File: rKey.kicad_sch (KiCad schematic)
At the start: 39 parts, among them IC1 BDX34C, J1 Conn_01x06, Q1 BC337, Q2 BC337, Q3 BC337, Q4 BC337, Q5 BC327, Q8 BC337, U1 TL084BCN, U2 LM7810_TO220

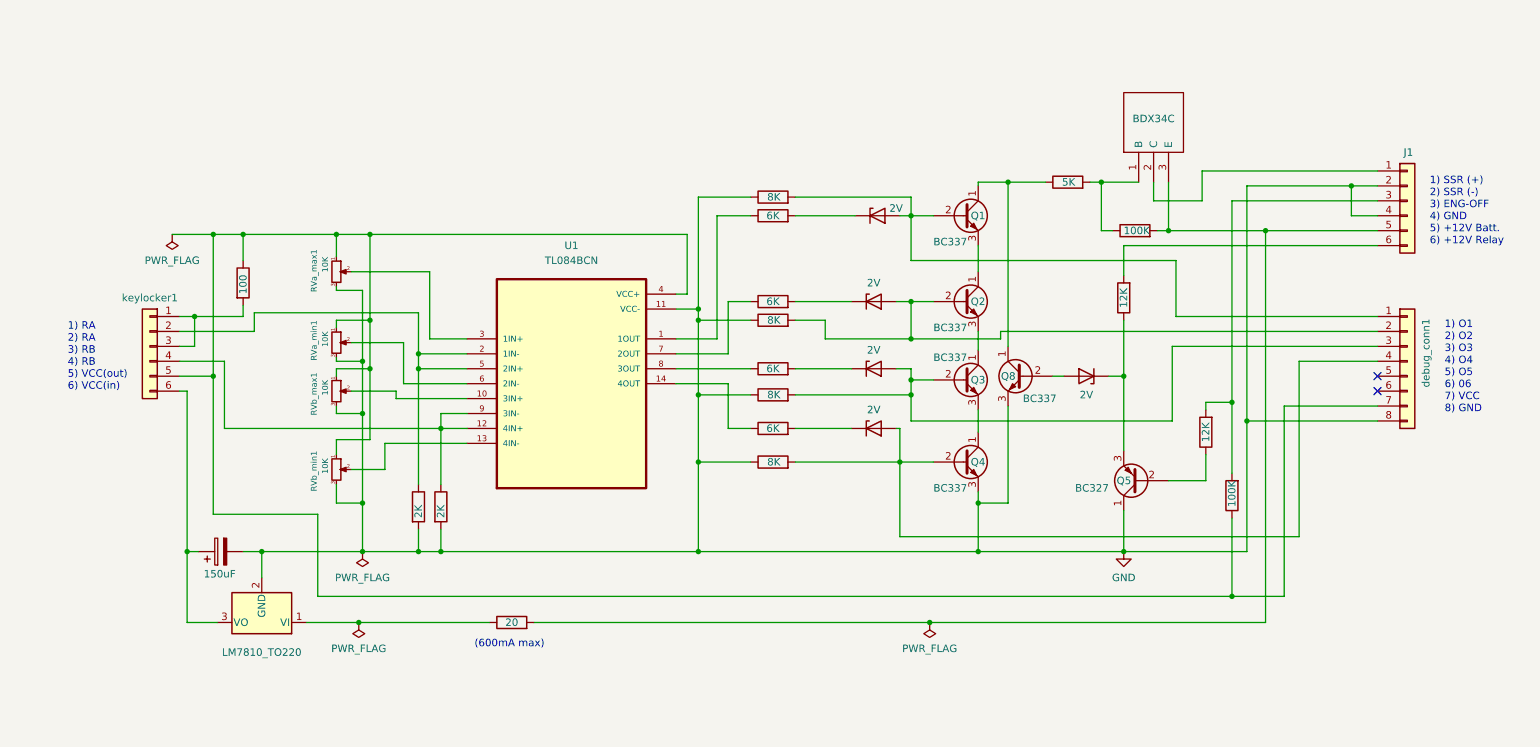
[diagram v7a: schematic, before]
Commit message: feat: Locking the engine when the vehicle is off
In order to forbid to manually run the engine when the vehicle is off, I added a NC micro relay.
PCB size has been reduced
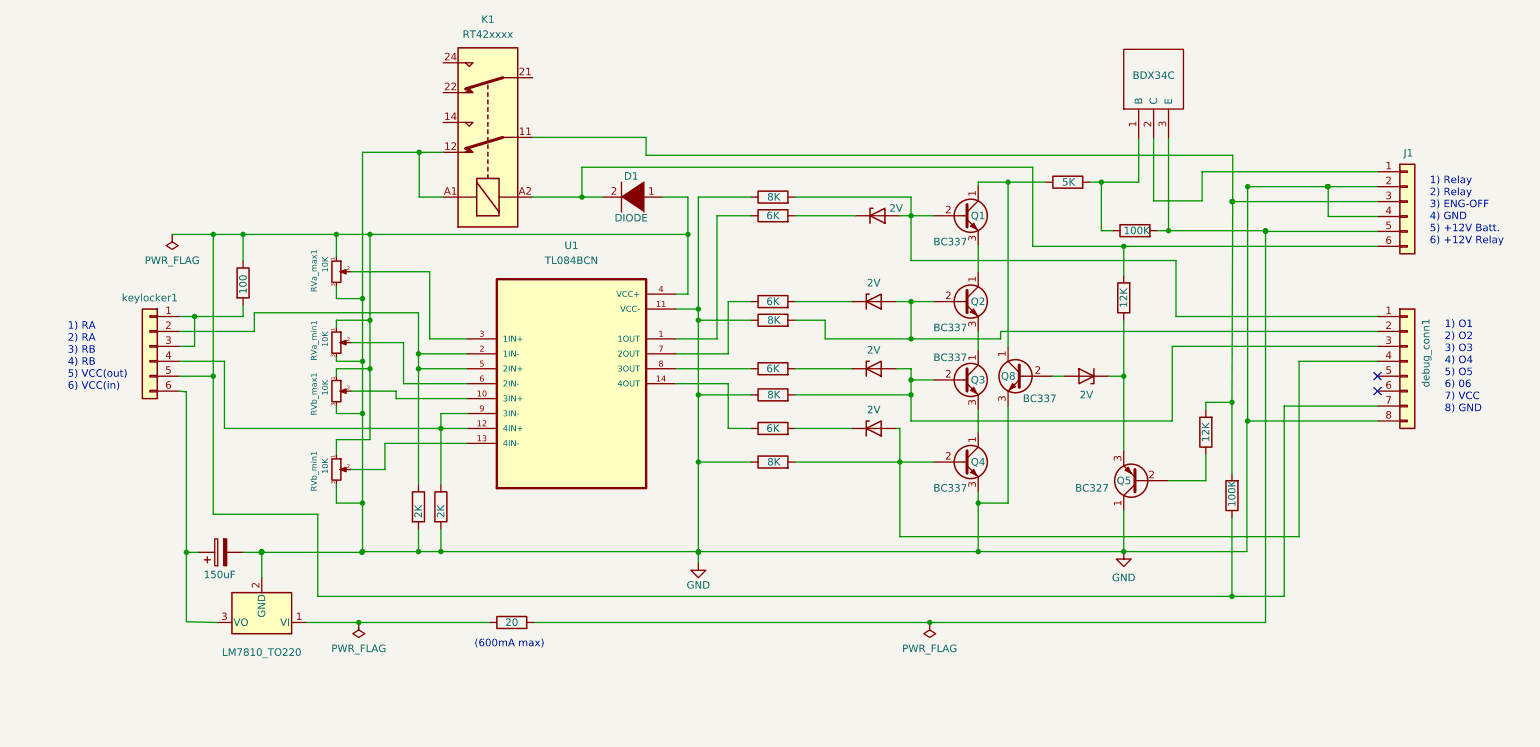
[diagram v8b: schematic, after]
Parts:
- added D1: DIODE, Diode_THT:D_DO-34_SOD68_P7.62mm_Horizontal, symbol pspice:DIODE
- added K1: RT42xxxx, Relay_THT:Relay_DPDT_Schrack-RT2-FormC_RM5mm, symbol Relay:RT42xxxx
- R10, R11, R12, R13, R15, R16, R17, R2, R3, R4, R5, R7, R8, R9: footprint Resistor_THT:R_Axial_DIN0207_L6.3mm_D2.5mm_P10.16mm_Horizontal -> Resistor_THT:R_Axial_DIN0204_L3.6mm_D1.6mm_P5.08mm_Horizontal
- R14: footprint Resistor_THT:R_Axial_DIN0207_L6.3mm_D2.5mm_P10.16mm_Horizontal -> Resistor_THT:R_Axial_DIN0204_L3.6mm_D1.6mm_P7.62mm_Horizontal
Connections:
- net GND: now also K1.12, K1.A1
- net at J1.3 (Pin_3), R13.2, R14.2: now also K1.11
- net at R1.1, R14.1, RVa_max1.1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: now also D1.1 (K)
- net at J1.6 (Pin_6), R9.2: now also D1.2 (A), K1.A2
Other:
- note added: "1) Relay 2) Relay 3) ENG-OFF 4) GND 5) +12V Batt. 6) +12V Relay"
- note removed: "1) SSR (+) 2) SSR (-) 3) ENG-OFF 4) GND 5) +12V Batt. 6) +12V Relay"
